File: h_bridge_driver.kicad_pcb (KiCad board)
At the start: 4 copper layers, 120 x 80 mm, 68 parts, among them IC1 DRV8702QRHBRQ1, J1 IN1, J2 IN2, J3 SUPP, J4 IN1, J5 IN1, J6 GND, Q1 SUD80460E, Q2 SUD80460E, Q3 SUD80460E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

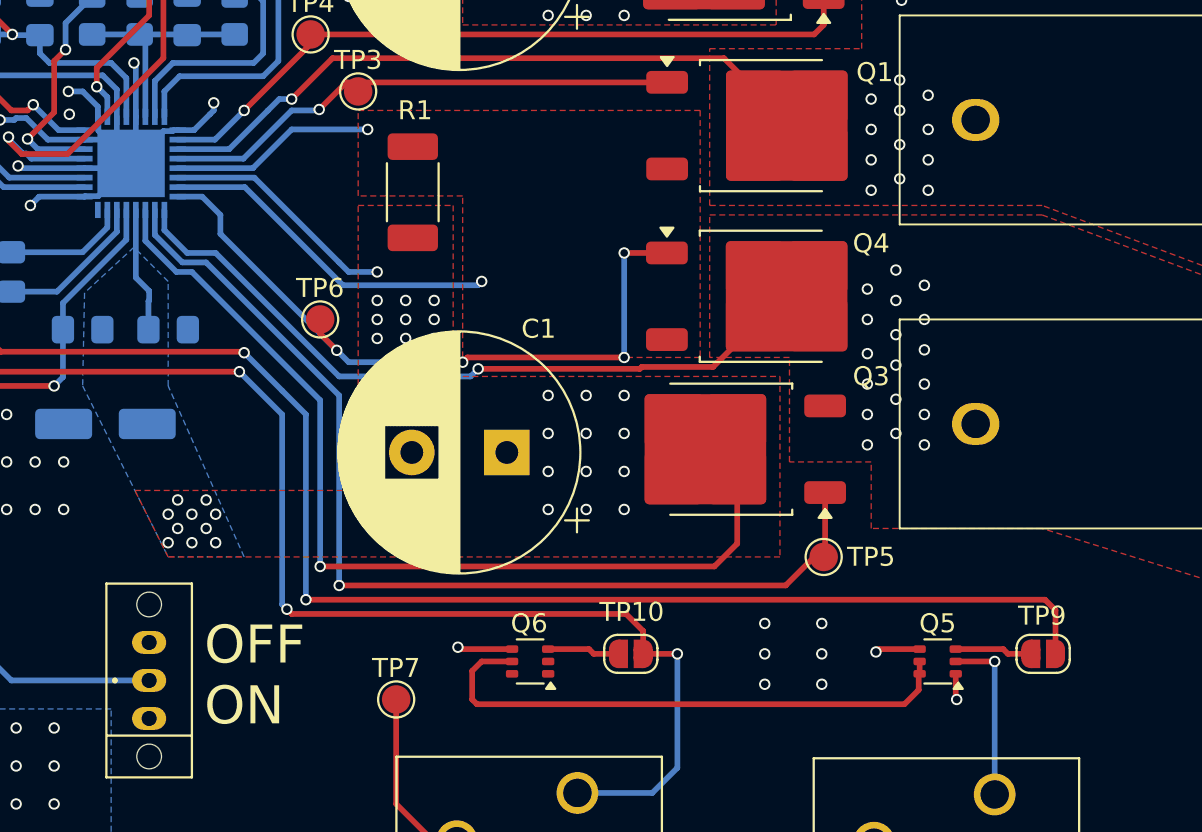
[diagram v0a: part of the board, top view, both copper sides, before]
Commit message: Fixed incorrect plane dimensions on power layer. Fixed wrong connection of BJT to RVP MOSFET gate.
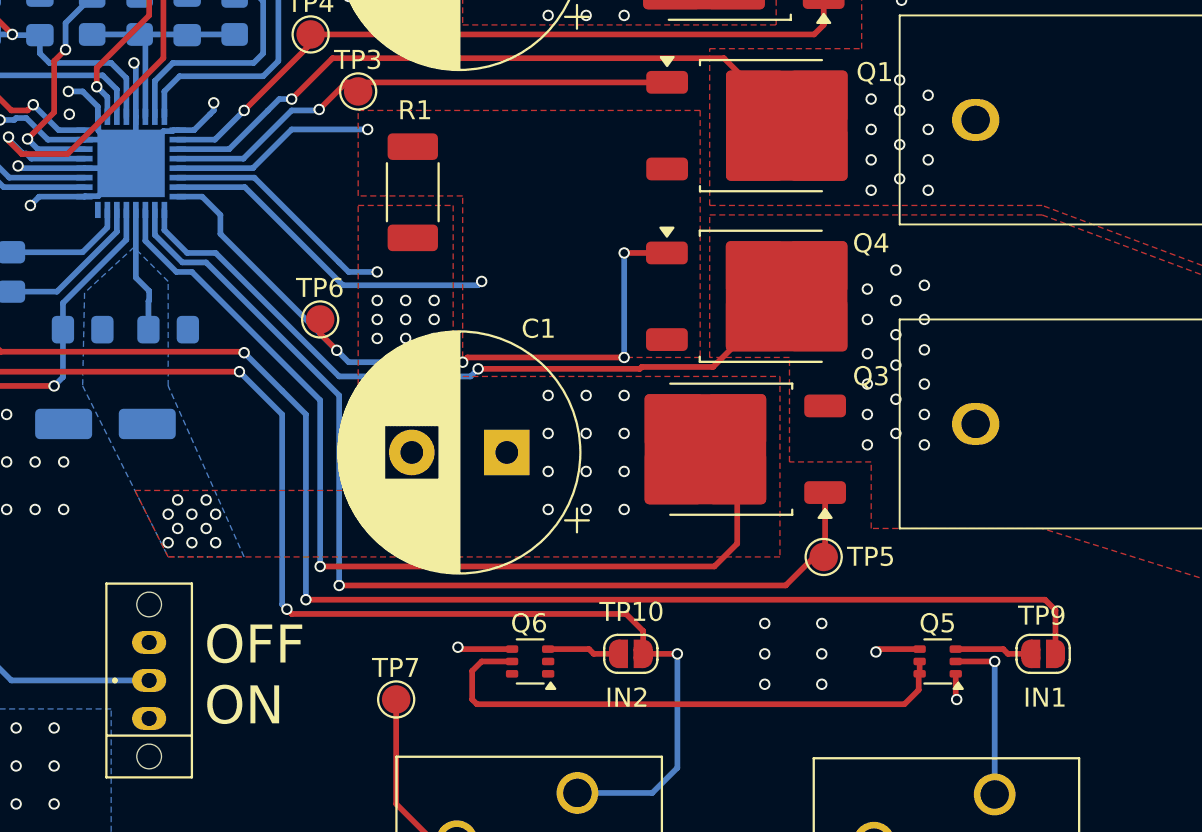
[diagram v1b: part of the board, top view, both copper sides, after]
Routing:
- net GND: track 55.4 -> 53.7 mm
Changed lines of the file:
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@@
 		)
 	)
+	(gr_text "IN2"
+		(at 156 106.5 0)
+		(layer "F.SilkS")
+		(effects
+			(font
+				(size 1 1)
+				(thickness 0.1)
+			)
+			(justify left bottom)
+		)
+	)
 	(gr_text "IN1"
 		(at 95.5 87 0)
@@
 		)
 	)
+	(gr_text "IN1"
+		(at 178 106.5 0)
+		(layer "F.SilkS")
+		(effects
+			(font
+				(size 1 1)
+				(thickness 0.1)
+			)
+			(justify left bottom)
+		)
+	)
 	(dimension
 		(type aligned)
@@
 	)
 	(segment
-		(start 130.3 75.3375)
-		(end 130.3 77.0375)
-		(width 0.3)
-		(layer "B.Cu")
-		(net 2)
-	)
-	(segment
 		(start 131.3 77.5375)
 		(end 131.05 77.7875)
@@
 		(polygon
 			(pts
-				(xy 117.5 130) (xy 127.5 130) (xy 127.5 98.5) (xy 161 98.5) (xy 161 70.2) (xy 117.5 70.2) (xy 117.5 105)
+				(xy 117.5 130) (xy 127.5 130) (xy 127.5 98.5) (xy 161 98.5) (xy 161 62.5) (xy 117.5 62.5) (xy 117.5 105)
 				(xy 117.5 107)
 			)
